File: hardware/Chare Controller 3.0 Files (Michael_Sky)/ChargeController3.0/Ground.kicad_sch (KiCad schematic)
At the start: 4 parts

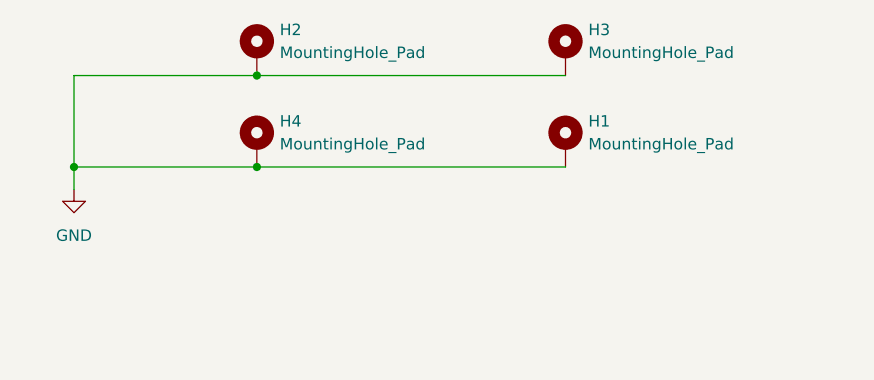
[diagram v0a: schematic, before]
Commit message: Grounding and Filtering, 3.0 Inhibits Updated
Grounding and Filtering, 3.0 Inhibits Updated
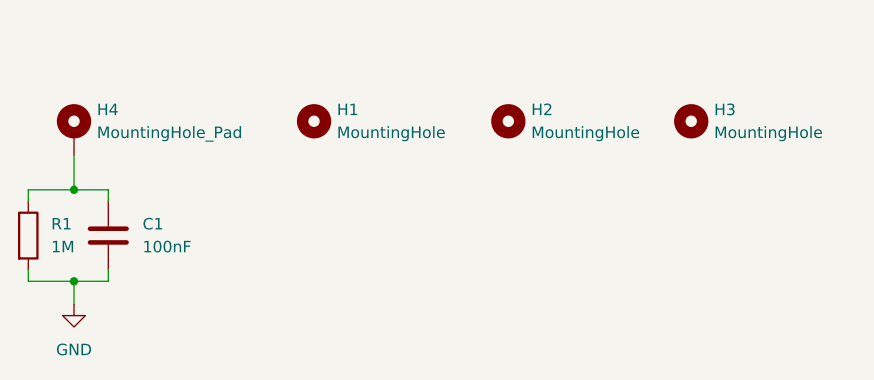
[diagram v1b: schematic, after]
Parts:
- removed H1, H2, H3: MountingHole_Pad, MountingHole:MountingHole_3.2mm_M3_ISO14580_Pad, symbol Mechanical:MountingHole_Pad
- added C1: 100nF, symbol Device:C
- added H1, H2, H3: MountingHole, symbol Mechanical:MountingHole
- added R1: 1M, symbol Device:R
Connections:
- net GND: now also C1.2, R1.2; no longer H4.1
- new net: C1.1, H4.1, R1.1
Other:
- moved on the sheet: H4
